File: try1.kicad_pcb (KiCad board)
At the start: 2 copper layers, 175.3 x 119.4 mm, 33 parts, among them J10 Archon-connector-modules-Driv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, J11 Archon-connector-modules-Driv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, J2 Archon-connector-modules-Heat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, J21 DB37, J22 DB37, J3 Archon-connector-modules-Driv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, J31 DB9, J4 Archon-connector-modules-LVBi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, J41 CONN_DVI, J5 Archon-connector-modules-ADC, J6 Archon-connector-modules-ADC, J7 Archon-connector-modules-ADC, J8 Archon-connector-modules-ADC, J9 Archon-connector-modules-HVBi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, P1 CONN_02X02

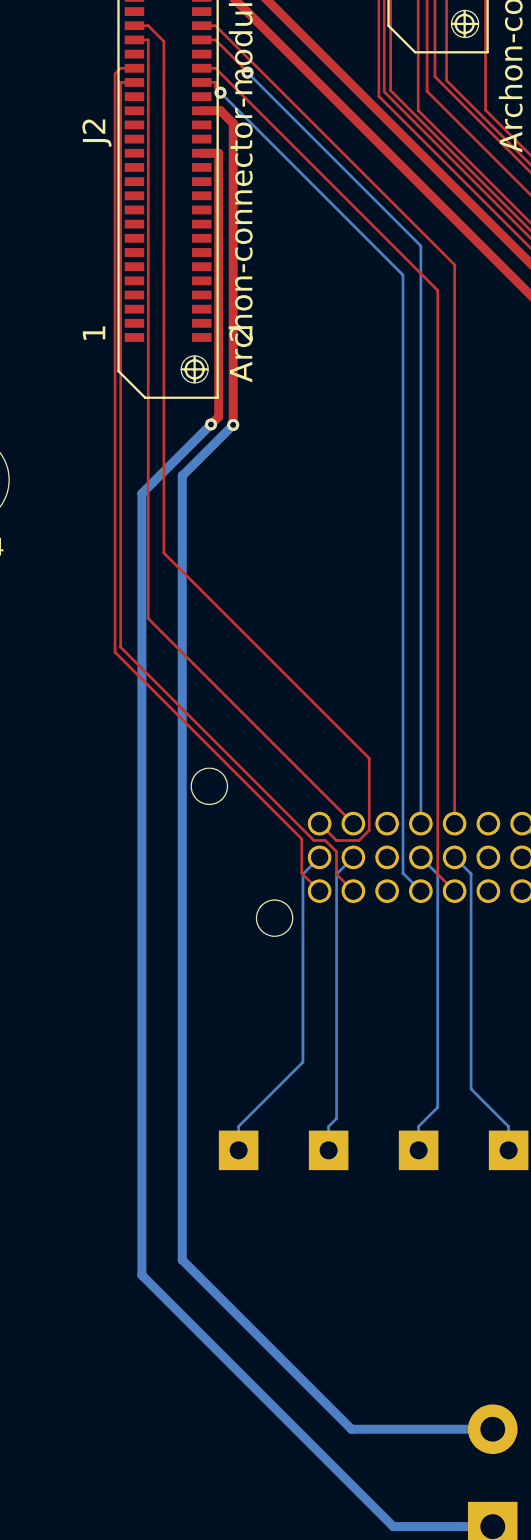
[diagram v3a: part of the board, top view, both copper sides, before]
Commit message: WIP: Move Heater Traces
Moved the heater traces a bit after noticing they were pretty close to the
pads.
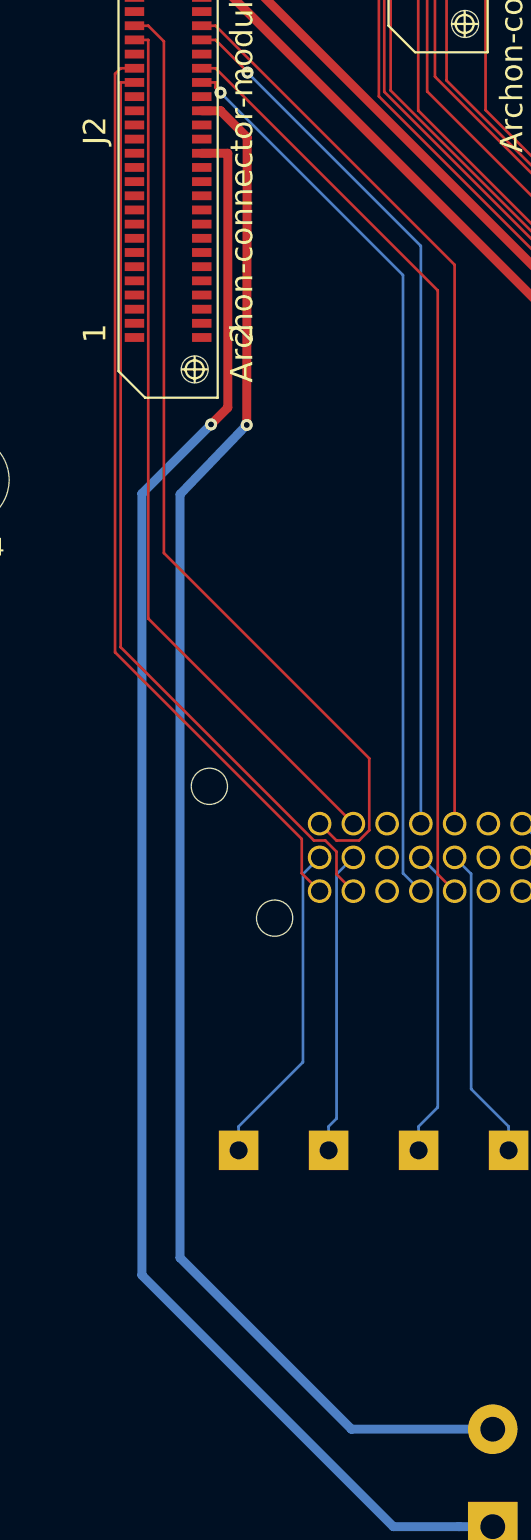
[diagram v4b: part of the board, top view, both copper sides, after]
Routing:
- net HEATER1_AP: track 91.8 -> 92.5 mm
- net HEATER1_AN: track 88.9 -> 89.6 mm
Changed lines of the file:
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@@
     (thickness 1.6)
     (drawings 7)
-    (tracks 624)
+    (tracks 623)
     (zones 0)
     (modules 33)
@@
   (segment (start 67.0225 65.7065) (end 63.121124 69.607876) (width 0.508) (layer B.Cu) (net 27))
   (segment (start 63.121124 113.72877) (end 77.314354 127.922) (width 0.508) (layer B.Cu) (net 27))
-  (segment (start 66.4999 50.3989) (end 67.4565 50.3989) (width 0.508) (layer F.Cu) (net 27))
-  (segment (start 67.4565 50.3989) (end 67.4565 65.2725) (width 0.508) (layer F.Cu) (net 27))
-  (segment (start 67.4565 65.2725) (end 67.0225 65.7065) (width 0.508) (layer F.Cu) (net 27))
+  (segment (start 66.4999 50.3989) (end 67.9704 50.3989) (width 0.508) (layer F.Cu) (net 27))
+  (segment (start 67.9704 50.3989) (end 67.9704 64.7586) (width 0.508) (layer F.Cu) (net 27))
+  (segment (start 67.9704 64.7586) (end 67.0225 65.7065) (width 0.508) (layer F.Cu) (net 27))
   (via (at 67.0225 65.7065) (size 0.6858) (layers F.Cu B.Cu) (net 27))
+  (segment (start 65.278 69.6468) (end 69.0372 65.7352) (width 0.508) (layer B.Cu) (net 33))
   (segment (start 82.9259 122.422) (end 74.9494 122.422) (width 0.508) (layer B.Cu) (net 33))
-  (segment (start 74.9494 122.422) (end 65.398649 112.871249) (width 0.508) (layer B.Cu) (net 33))
-  (segment (start 65.398649 112.871249) (end 65.398649 68.586351) (width 0.508) (layer B.Cu) (net 33))
-  (segment (start 65.398649 68.586351) (end 65.424049 68.586351) (width 0.508) (layer B.Cu) (net 33))
-  (segment (start 65.424049 68.586351) (end 68.2752 65.7352) (width 0.508) (layer B.Cu) (net 33))
-  (segment (start 68.2752 65.7352) (end 68.2752 48.71849) (width 0.508) (layer F.Cu) (net 33))
-  (segment (start 68.2752 48.71849) (end 67.55783 48.00112) (width 0.508) (layer F.Cu) (net 33))
-  (via (at 68.2752 65.7352) (size 0.6858) (drill 0.3302) (layers F.Cu B.Cu) (net 33))
+  (segment (start 74.9494 122.422) (end 65.271649 112.744249) (width 0.508) (layer B.Cu) (net 33))
+  (segment (start 65.271649 112.744249) (end 65.271649 69.653151) (width 0.508) (layer B.Cu) (net 33))
+  (segment (start 69.0372 65.7352) (end 69.062327 49.504678) (width 0.508) (layer F.Cu) (net 33))
+  (segment (start 69.062327 49.504678) (end 67.55783 48.00112) (width 0.508) (layer F.Cu) (net 33))
+  (via (at 69.0372 65.7352) (size 0.6858) (drill 0.3302) (layers F.Cu B.Cu) (net 33))
   (segment (start 66.49992 48.00112) (end 67.55783 48.00112) (width 0.508) (layer F.Cu) (net 33))
   (segment (start 67.55783 48.00112) (end 67.56271 48.006) (width 0.508) (layer F.Cu) (net 33))

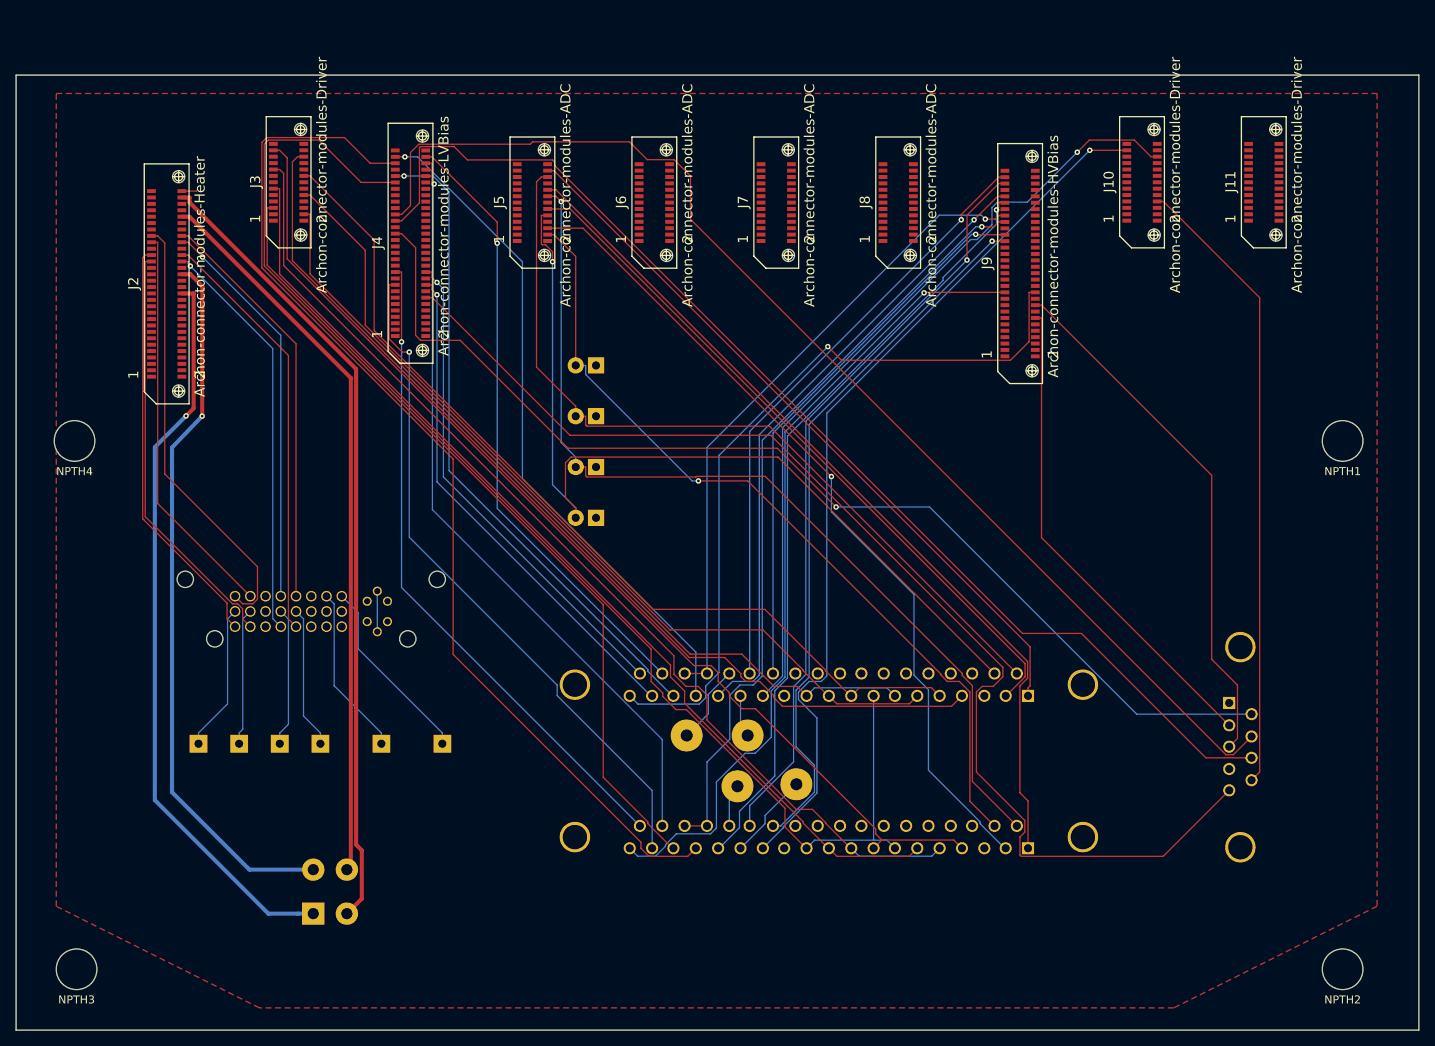
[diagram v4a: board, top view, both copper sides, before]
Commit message: Delete Old DRV Traces
After updating the schematic and exporting the new netlist, I updated the
PCB.  I thought this would delete all the old traces, but I had to do some
of that myself.  In any case, I think this is ready for me to route the
new assignments for the driver modules.
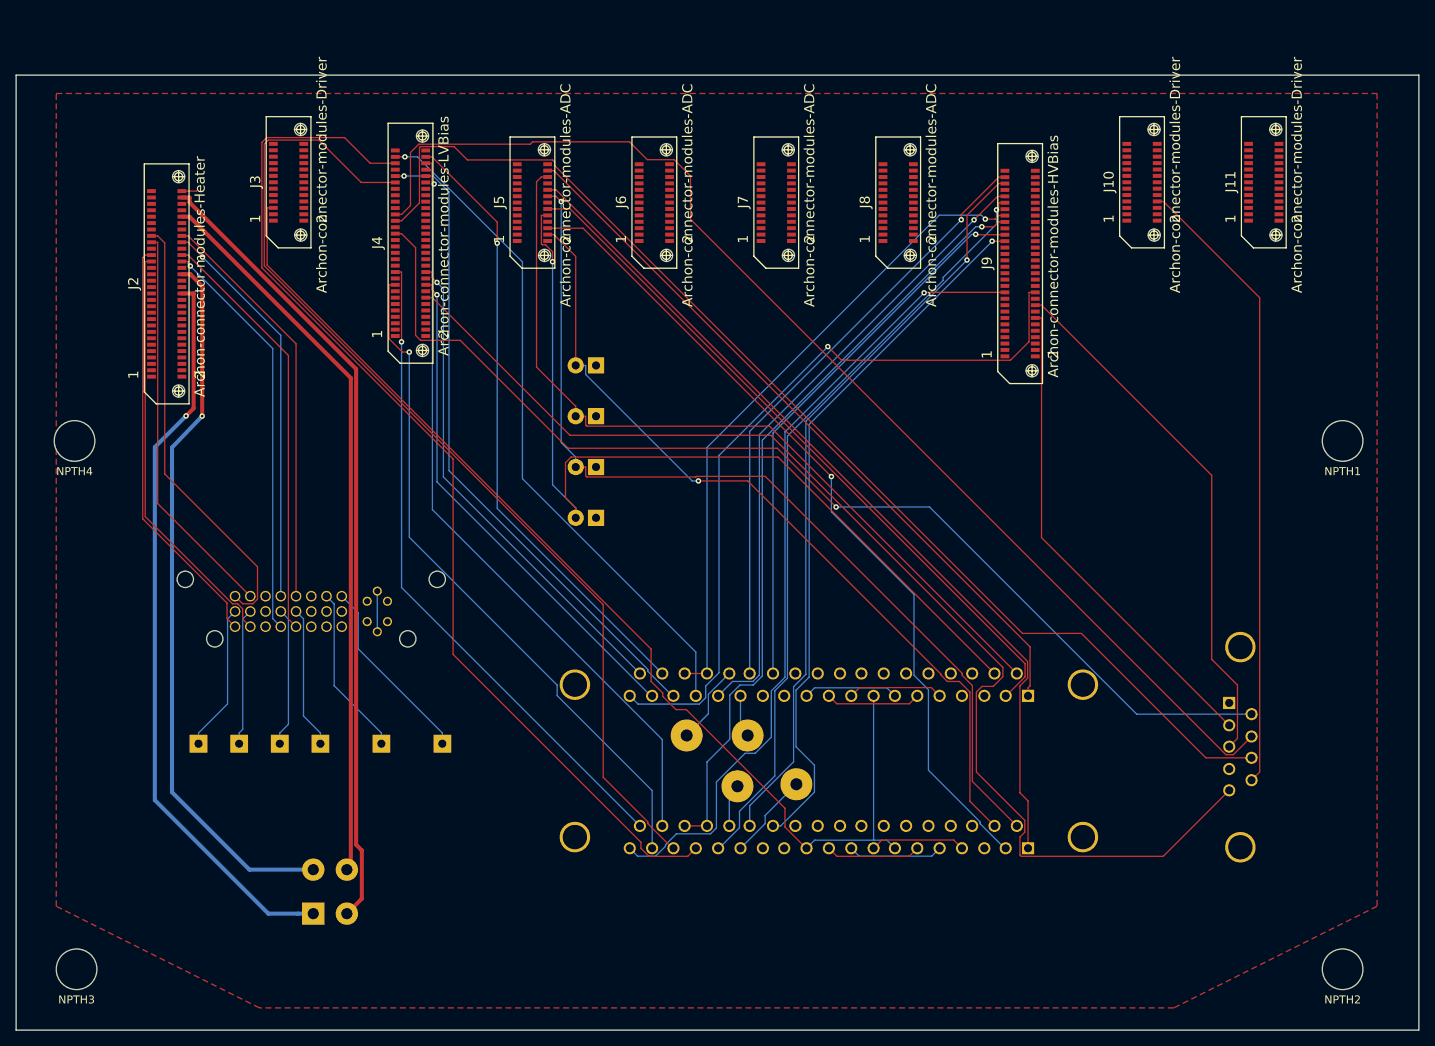
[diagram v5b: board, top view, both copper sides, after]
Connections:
- net Net-(J11-Pad10) renamed DRV11_CH5
- net Net-(J11-Pad11) renamed DRV11_CH6
- net Net-(J11-Pad16) renamed DRV11_CH3
- net Net-(J11-Pad4) renamed DRV11_CH7
- net Net-(J11-Pad5) renamed DRV11_CH8
- J10 pad 10: Net-(J10-Pad10) -> DRV10_CH5
- J10 pad 11: Net-(J10-Pad11) -> DRV10_CH6
- J10 pad 16: Net-(J10-Pad16) -> DRV10_CH3
- J10 pad 17: Net-(J10-Pad17) -> DRV10_CH4
- J10 pad 25: Net-(J10-Pad25) -> /GND
- J10 pad 26: Net-(J10-Pad26) -> /GND
- J10 pad 4: Net-(J10-Pad4) -> DRV10_CH7
- J10 pad 5: Net-(J10-Pad5) -> DRV10_CH8
- J10 pad 8: DRV10_CH8 -> Net-(J10-Pad8)
- J11 pad 17: Net-(J11-Pad17) -> DRV11_CH4
- J11 pad 22: Net-(J11-Pad22) -> DRV11_CH1
- J11 pad 23: Net-(J11-Pad23) -> DRV11_CH2
- J11 pad 25: Net-(J11-Pad25) -> /GND
- J11 pad 26: Net-(J11-Pad26) -> /GND
- J21 pad 10: DRV3_CH6 -> DRV3_CH7
- J21 pad 11: DRV3_CH8 -> DRV3_CH6
- J21 pad 13: DRV10_CH2 -> DRV3_CH2
- J21 pad 4: DRV3_CH2 -> DRV11_CH2
- J21 pad 5: DRV3_CH4 -> DRV10_CH3
- J21 pad 6: DRV3_CH6 -> DRV10_CH7
- J21 pad 7: DRV3_CH8 -> DRV10_CH6
- J21 pad 8: DRV3_CH2 -> DRV10_CH2
- J21 pad 9: DRV3_CH4 -> DRV3_CH3
- J22 pad 11: DRV3_CH7 -> DRV3_CH8
- J22 pad 13: DRV10_CH1 -> DRV3_CH4
- J22 pad 4: DRV3_CH1 -> DRV11_CH4
- J22 pad 5: DRV3_CH3 -> DRV10_CH1
- J22 pad 6: DRV3_CH5 -> DRV10_CH5
- J22 pad 7: DRV3_CH7 -> DRV10_CH8
- J22 pad 8: DRV3_CH8 -> DRV10_CH4
- J22 pad 9: DRV3_CH3 -> DRV3_CH1
- J3 pad 25: Net-(J3-Pad25) -> /GND
- J3 pad 26: Net-(J3-Pad26) -> /GND
- J31 pad 9: DRV10_CH8 -> DRV11_CH1
- J5 pad 25: Net-(J5-Pad25) -> /GND
- J5 pad 26: Net-(J5-Pad26) -> /GND
- J9 pad 59: Net-(J9-Pad59) -> /GND
- J9 pad 60: Net-(J9-Pad60) -> /GND
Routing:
- net DRV3_CH2: track 132.3 -> 0.00 mm
- net DRV3_CH4: track 129.2 -> 0.00 mm
- net DRV3_CH8: track 139.5 -> 11.2 mm
- net DRV3_CH1: track 121.7 -> 1.53 mm
- net DRV3_CH3: track 113.9 -> 1.48 mm
- net DRV3_CH5: track 109.0 -> 1.48 mm
- net DRV3_CH7: track 104.0 -> 1.50 mm
- net DRV10_CH2: track 111.6 -> 10.4 mm, vias 1 -> 0
- net DRV10_CH1: track 98.4 -> 10.4 mm, vias 1 -> 0
- net DRV11_CH1: track 0.00 -> 77.7 mm
- net DRV10_CH8: track 78.5 -> 1.42 mm
- net DRV10_CH4: track 0.00 -> 27.0 mm
- net DRV3_CH6: track 123.6 -> 110.2 mm
- net DRV10_CH3: track 0.00 -> 10.5 mm
- net DRV10_CH5: track 0.00 -> 10.5 mm
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
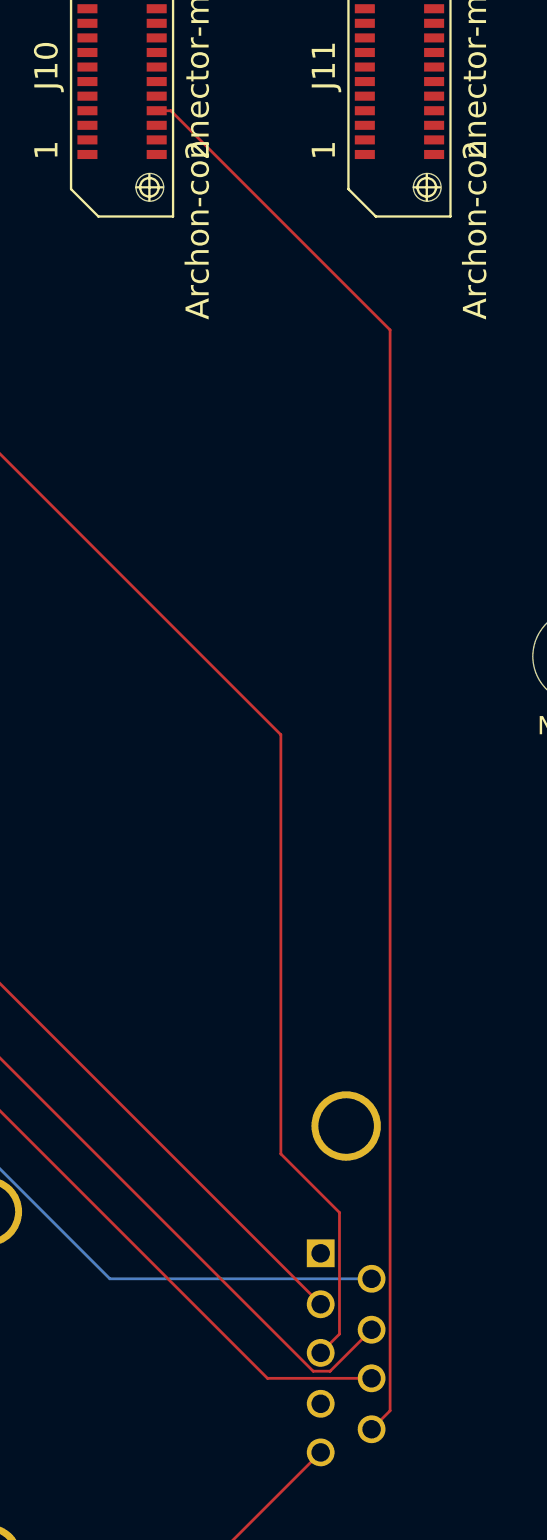
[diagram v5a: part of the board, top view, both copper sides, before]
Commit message: Deleted another old trace
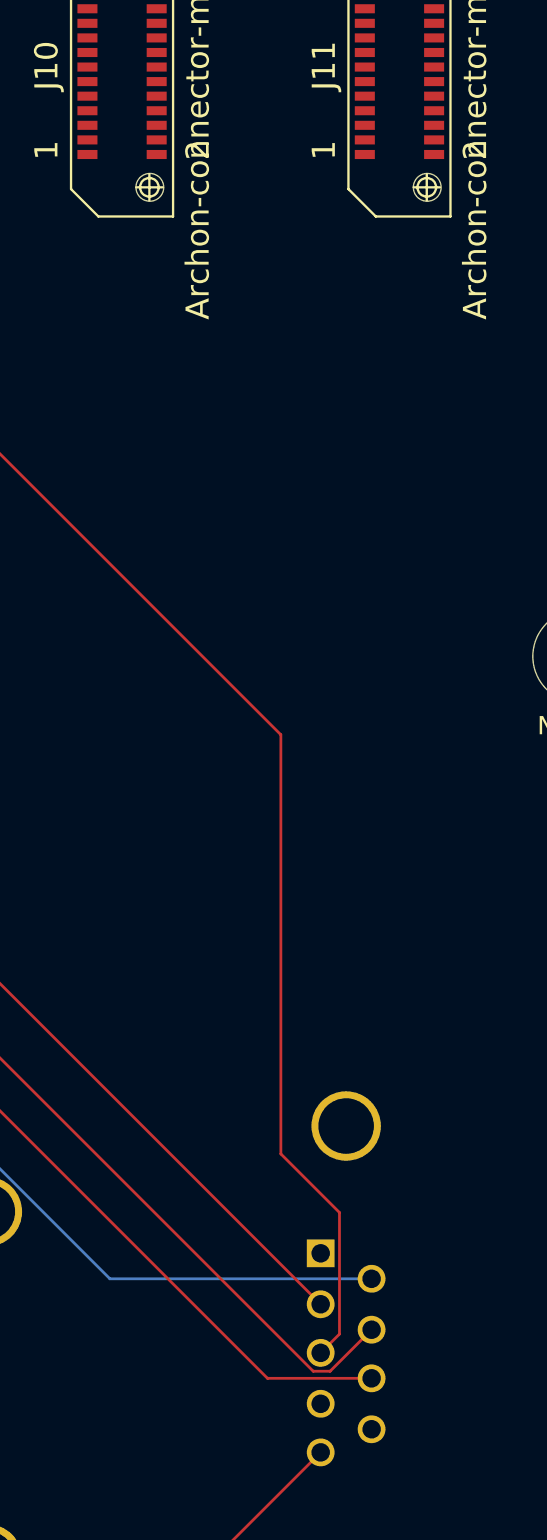
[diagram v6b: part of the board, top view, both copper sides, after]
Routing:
- net DRV11_CH1: track 77.7 -> 0.00 mm
- net Net-(J10-Pad8): track 0.78 -> 0.00 mm
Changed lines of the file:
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@@
     (thickness 1.6)
     (drawings 7)
-    (tracks 522)
+    (tracks 518)
     (zones 0)
     (modules 33)
@@
   (segment (start 157.42 120.756) (end 158.429 119.747) (width 0.1524) (layer F.Cu) (net 356))
   (segment (start 148.388 120.756) (end 157.42 120.756) (width 0.1524) (layer F.Cu) (net 356))
-  (segment (start 188.42 38.8978) (end 189.199 38.8978) (width 0.1524) (layer F.Cu) (net 357))
   (segment (start 188.42 38.8978) (end 188.4199 38.8978) (width 0.1524) (layer F.Cu) (net 357))
   (segment (start 157.436 101.69) (end 158.429 100.697) (width 0.1524) (layer F.Cu) (net 358))
@@
   (segment (start 145.603 118.73) (end 152.968 118.73) (width 0.1524) (layer B.Cu) (net 361))
   (segment (start 152.968 118.73) (end 154.618 118.73) (width 0.1524) (layer B.Cu) (net 361))
-  (segment (start 201.226 110.224) (end 200.212 111.238) (width 0.1524) (layer F.Cu) (net 368))
-  (segment (start 201.226 50.9253) (end 201.226 110.224) (width 0.1524) (layer F.Cu) (net 368))
-  (segment (start 189.199 38.8978) (end 201.226 50.9253) (width 0.1524) (layer F.Cu) (net 368))
   (segment (start 162.986 118.716) (end 164.017 119.747) (width 0.1524) (layer F.Cu) (net 369))
   (zone (net 23) (net_name /GND) (layer F.Cu) (hatch edge 0.508)
